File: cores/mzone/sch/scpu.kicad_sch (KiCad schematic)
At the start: 77 parts, among them X1 14.318MHZ

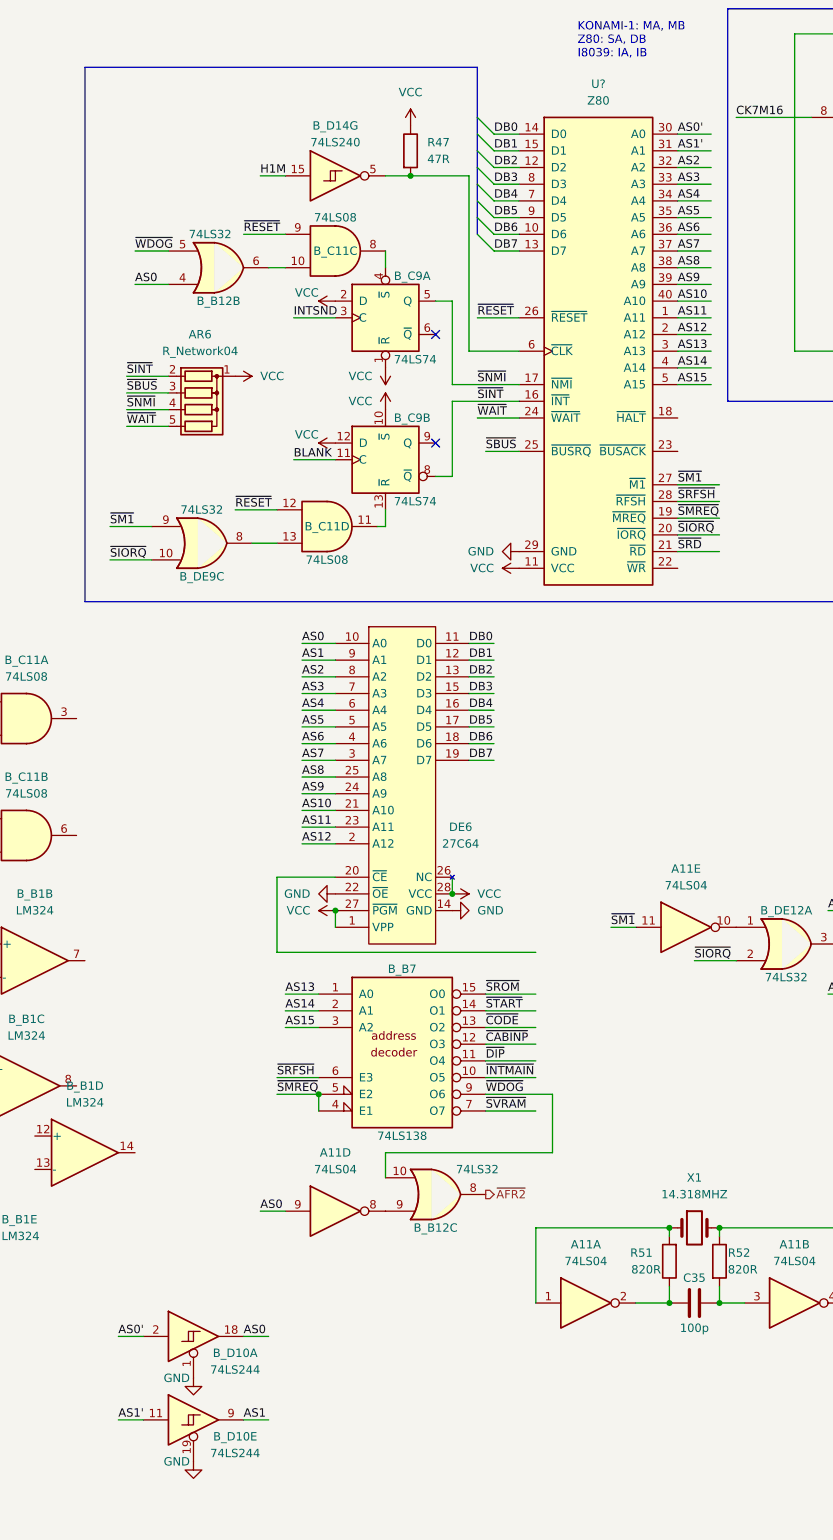
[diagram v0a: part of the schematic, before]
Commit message: mzone core
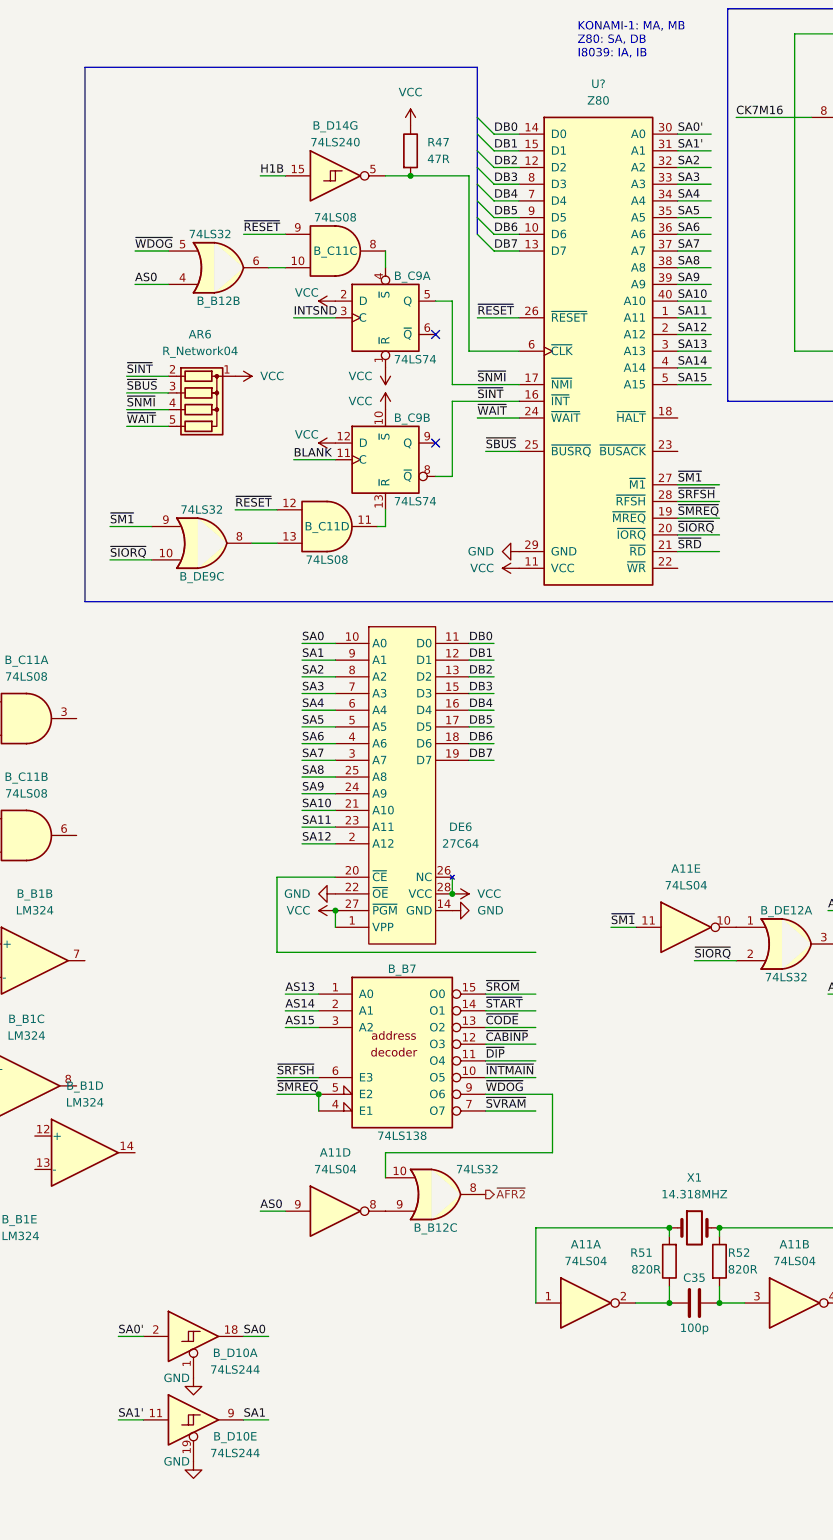
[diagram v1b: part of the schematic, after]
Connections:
- net AS0: no longer B_D10.18, DE6.10 (A0)
- net AS1: no longer B_D10.9, DE6.9 (A1)
- net AS13: no longer U?.3 (A13)
- net AS14: no longer U?.4 (A14)
- net AS15: no longer U?.5 (A15)
- net AS0' renamed SA0'
- net AS1' renamed SA1'
- net AS10 renamed SA10
- net AS11 renamed SA11
- net AS12 renamed SA12
- net AS2 renamed SA2
- net AS3 renamed SA3
- net AS4 renamed SA4
- net AS5 renamed SA5
- net AS6 renamed SA6
- net AS7 renamed SA7
- net AS8 renamed SA8
- net AS9 renamed SA9
- net H1M renamed H1B
- new net SA0: B_D10.18, DE6.10 (A0)
- new net SA1: B_D10.9, DE6.9 (A1)
- new net SA13: U?.3 (A13)
- new net SA14: U?.4 (A14)
- new net SA15: U?.5 (A15)
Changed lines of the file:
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@@
 		)
 	)
-	(label "AS8"
+	(label "SA8"
 		(at 58.42 128.27 0)
 		(effects
@@
 		)
 	)
-	(label "AS13"
+	(label "SA13"
 		(at 115.57 63.5 0)
 		(effects
@@
 		)
 	)
-	(label "AS3"
+	(label "SA3"
 		(at 115.57 38.1 0)
 		(effects
@@
 		)
 	)
-	(label "AS4"
+	(label "SA4"
 		(at 58.42 118.11 0)
 		(effects
@@
 		)
 	)
-	(label "AS2"
+	(label "SA2"
 		(at 58.42 113.03 0)
 		(effects
@@
 		)
 	)
-	(label "AS12"
+	(label "SA12"
 		(at 115.57 60.96 0)
 		(effects
@@
 		)
 	)
-	(label "AS3"
+	(label "SA3"
 		(at 58.42 115.57 0)
 		(effects
@@
 		)
 	)
-	(label "AS12"
+	(label "SA12"
 		(at 58.42 138.43 0)
 		(effects
@@
 		)
 	)
-	(label "AS15"
+	(label "SA15"
 		(at 115.57 68.58 0)
 		(effects
@@
 		)
 	)
-	(label "AS6"
+	(label "SA6"
 		(at 115.57 45.72 0)
 		(effects
@@
 		)
 	)
-	(label "AS0"
+	(label "SA0"
 		(at 58.42 107.95 0)
 		(effects
@@
 		)
 	)
-	(label "AS5"
+	(label "SA5"
 		(at 58.42 120.65 0)
 		(effects
@@
 		)
 	)
-	(label "AS1"
+	(label "SA1"
 		(at 58.42 110.49 0)
 		(effects
@@
 		)
 	)
-	(label "AS10"
+	(label "SA10"
 		(at 115.57 55.88 0)
 		(effects
@@
 		)
 	)
-	(label "AS8"
+	(label "SA8"
 		(at 115.57 50.8 0)
 		(effects
@@
 		)
 	)
-	(label "AS1'"
+	(label "SA1'"
 		(at 30.48 226.06 0)
 		(effects
@@
 		)
 	)
-	(label "AS9"
+	(label "SA9"
 		(at 58.42 130.81 0)
 		(effects
@@
 		)
 	)
-	(label "AS7"
+	(label "SA7"
 		(at 115.57 48.26 0)
 		(effects
@@
 		)
 	)
-	(label "AS5"
+	(label "SA5"
 		(at 115.57 43.18 0)
 		(effects
@@
 		)
 	)
-	(label "AS6"
+	(label "SA6"
 		(at 58.42 123.19 0)
 		(effects
@@
 		)
 	)
-	(label "AS11"
+	(label "SA11"
 		(at 115.57 58.42 0)
 		(effects
@@
 		)
 	)
-	(label "AS7"
+	(label "SA7"
 		(at 58.42 125.73 0)
 		(effects
@@
 		)
 	)
-	(label "AS9"
+	(label "SA9"
 		(at 115.57 53.34 0)
 		(effects
@@
 		)
 	)
-	(label "AS10"
+	(label "SA10"
 		(at 58.42 133.35 0)
 		(effects
@@
 		)
 	)
-	(label "H1M"
+	(label "H1B"
 		(at 52.07 36.83 0)
 		(effects
@@
 		)
 	)
-	(label "AS14"
+	(label "SA14"
 		(at 115.57 66.04 0)
 		(effects
@@
 		)
 	)
-	(label "AS2"
+	(label "SA2"
 		(at 115.57 35.56 0)
 		(effects
@@
 		)
 	)
-	(label "AS1'"
+	(label "SA1'"
 		(at 115.57 33.02 0)
 		(effects
@@
 		)
 	)
-	(label "AS11"
+	(label "SA11"
 		(at 58.42 135.89 0)
 		(effects
@@
 		)
 	)
-	(label "AS0'"
+	(label "SA0'"
 		(at 30.48 213.36 0)
 		(effects
@@
 		)
 	)
-	(label "AS1"
+	(label "SA1"
 		(at 49.53 226.06 0)
 		(effects
@@
 		)
 	)
-	(label "AS4"
+	(label "SA4"
 		(at 115.57 40.64 0)
 		(effects
@@
 		)
 	)
-	(label "AS0'"
+	(label "SA0'"
 		(at 115.57 30.48 0)
 		(effects
@@
 		)
 	)
-	(label "AS0"
+	(label "SA0"
 		(at 49.53 213.36 0)
 		(effects

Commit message: mzone core
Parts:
- removed B_A2: 74LS373, symbol 74xx:74LS373
- added B_A2: 74LS373, symbol jt74:74LS373
- added unit 5 of B_C11
- B_B6: renamed from B_B1; value LM324 -> M5224P
- B_B6: value LM324 -> M5224P
- RA6: renamed from AR6; value R_Network04 -> 4.7k x 4
- gave numbers to parts that had none: 1
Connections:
- net AS0 is gone; now on net SA0: A11.9, B_B12.4, B_DE11.11
- net AS1 is gone; now on net SA1: B_DE11.2
- net AS13 is gone; now on net SA13: B_B7.1 (A0)
- net AS14 is gone; now on net SA14: B_B7.2 (A1)
- net AS15 is gone; now on net SA15: B_B7.3 (A2)
- net +12V: now also B_B6.4 (V+)
- net GND: now also A6.7 (VSS), B_A12.7 (GND), B_A5.7 (VSS), B_B10.7 (GND), B_B11.7 (GND), B_B6.11 (V-), B_B9.7 (GND), B_A2.1 (~{OE}), B_A2.10 (GND), B_C11.7 (GND)
- net IA0: now also B_A2.12 (O4)
- net IA1: now also B_A2.9 (O3)
- net IA2: now also B_A2.15 (O5)
- net IA3: now also B_A2.6 (O2)
- net IA4: now also B_A2.16 (O6)
- net IA5: now also B_A2.5 (O1)
- net IA6: now also B_A2.19 (O7)
- net IA7: now also B_A2.2 (O0)
- net VCC: now also A6.14 (VDD), B_A12.14 (VCC), B_A5.14 (VDD), B_B10.14 (VCC), B_B11.14 (VCC), B_B9.14 (VCC), B_A2.20 (VCC), B_C11.14 (VCC)
- net ~{SROM}: now also DE6.20 (~{CE})
- net at B_B4.11 (ALE): now also B_A2.11 (LE)
- net IAD0 renamed ID0
- net ID0: now also B_A2.13 (D4)
- net IAD1 renamed ID1
- net ID1: now also B_A2.8 (D3)
- net IAD2 renamed ID2
- net ID2: now also B_A2.14 (D5)
- net IAD3 renamed ID3
- net ID3: now also B_A2.7 (D2)
- net IAD4 renamed ID4
- net ID4: now also B_A2.17 (D6)
- net IAD5 renamed ID5
- net ID5: now also B_A2.4 (D1)
- net IAD6 renamed ID6
- net ID6: now also B_A2.18 (D7)
- net IAD7 renamed ID7
- net ID7: now also B_A2.3 (D0)
- net SA0': no longer names the net of B_D10.2, B_E7.30 (A0)
- net SA1': no longer names the net of B_D10.11, B_E7.31 (A1)
- no-connect marks 16 -> 54
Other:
- note added: "KONAMI-1: MA, MD Z80: SA, DB I8039: IA, ID"
- note removed: "KONAMI-1: MA, MB Z80: SA, DB I8039: IA, IB"
- note removed: "add to jt, remove power pins"
- note removed: "~{EA} cant be connected SS?"
- moved on the sheet: A6E, B_A12B, B_A5A, B_A5B, B_A5C, B_A5D, B_A5E, B_B10B, B_B11B, B_B12B, B_B6B, B_B6C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
